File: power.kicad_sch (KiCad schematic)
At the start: 20 parts

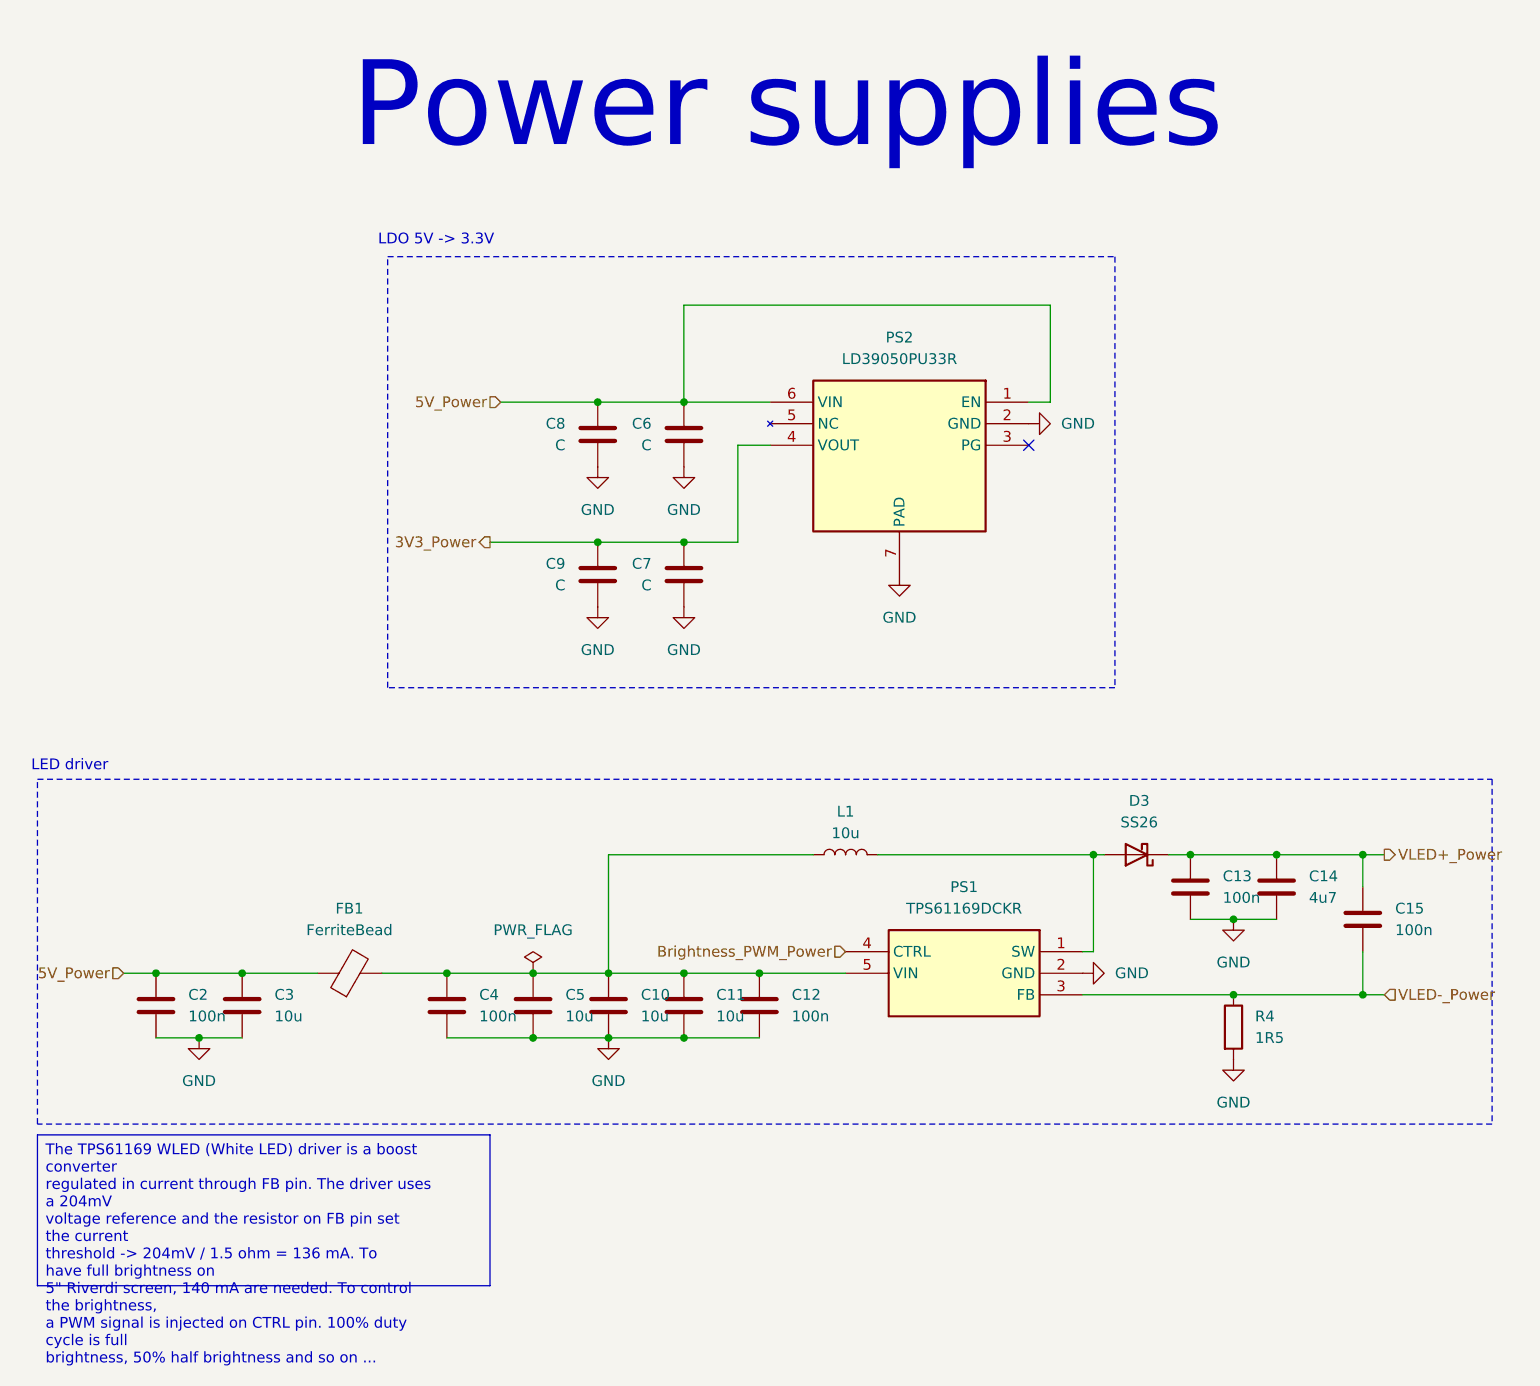
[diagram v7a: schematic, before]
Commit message: Add status LED for MCU and power supplies
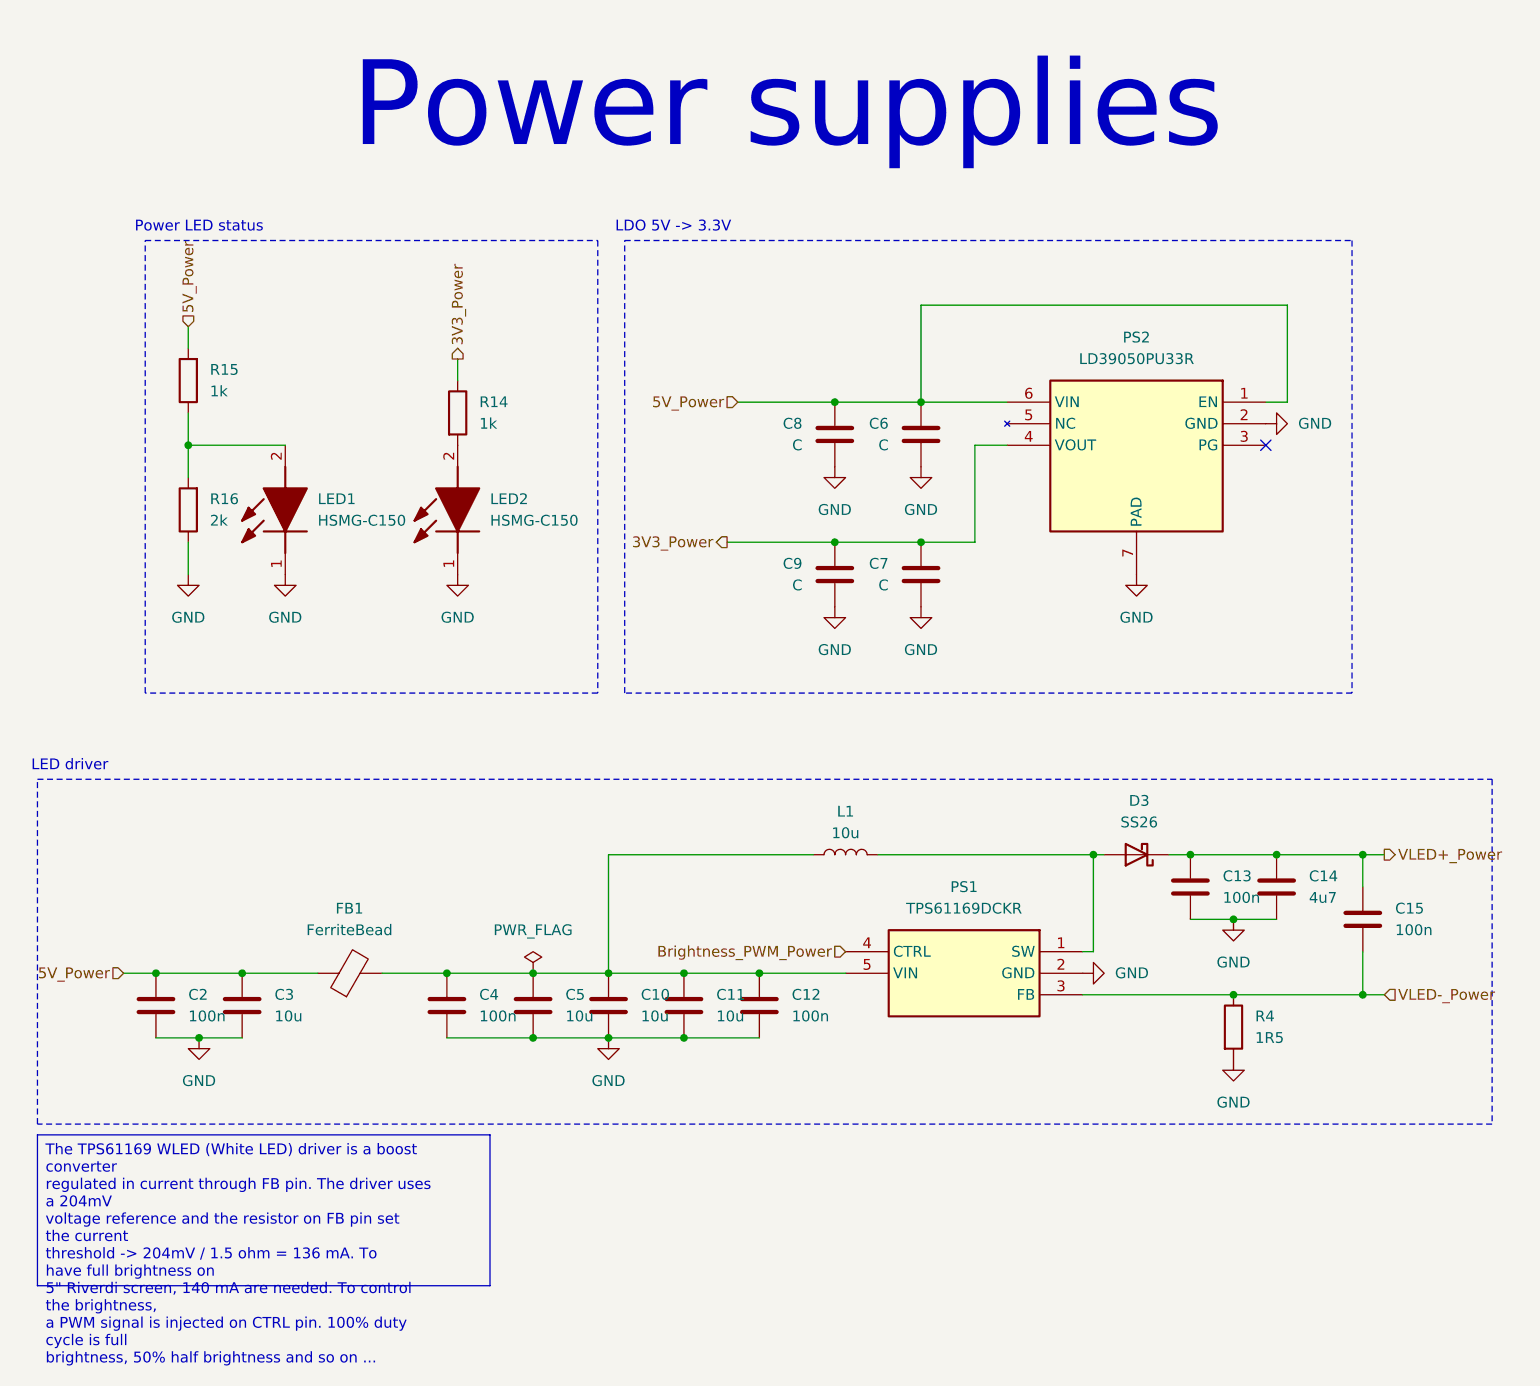
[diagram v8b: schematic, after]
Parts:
- added LED1, LED2: HSMG-C150, LEDC3216X120N, symbol weather-station-poc-sym:HSMG-C150
- added R14, R15: 1k, symbol Device:R
- added R16: 2k, symbol Device:R
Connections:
- net 3V3_Power: now also R14.1
- net 5V_Power: now also R15.2
- net GND: now also LED1.1 (K), LED2.1 (K), R16.1
- new net: LED1.2 (A), R15.1, R16.2
- new net: LED2.2 (A), R14.2
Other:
- note added: "Power LED status"
- moved on the sheet: C6, C7, C8, C9, PS2
